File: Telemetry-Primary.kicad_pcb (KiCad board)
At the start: 2 copper layers, 95 x 82 mm, 153 parts, among them J1 CAN_LogicAnalyzer, J10 SMAConn, J11 CAN_In, J12 CAN_Out, J2 IMU_LogicAnalyzer, J3 GPS_LogicAnalyzer, J4 SWD, J5 SDCard_LogicAnalyzer, J6 USB_B_Micro, J7 PowerConn, J8 RJ45_Abracon_ARJP11A-MASA-B-A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, J9 Micro_SD_Card_Det, SW1 Reset, SW2 RTCC_BattCheck, SW3 GPS_BattCheck, U1 STM32F429ZITx, U10 RN4871-I, U11 LAN8742A-CZ-TR, U12 USBLC6-4SC6, U2 RI3-1205S, U3 LD1117-3.3_SOT223, U4 ADM3055E, U5 CDSOT23-T24CAN, U6 BNO055, U7 MTK3339, U8 CP2102N-A02-GQFN24, U9 MCP112, Y1 8M, Y2 25M, Y3 32.768k

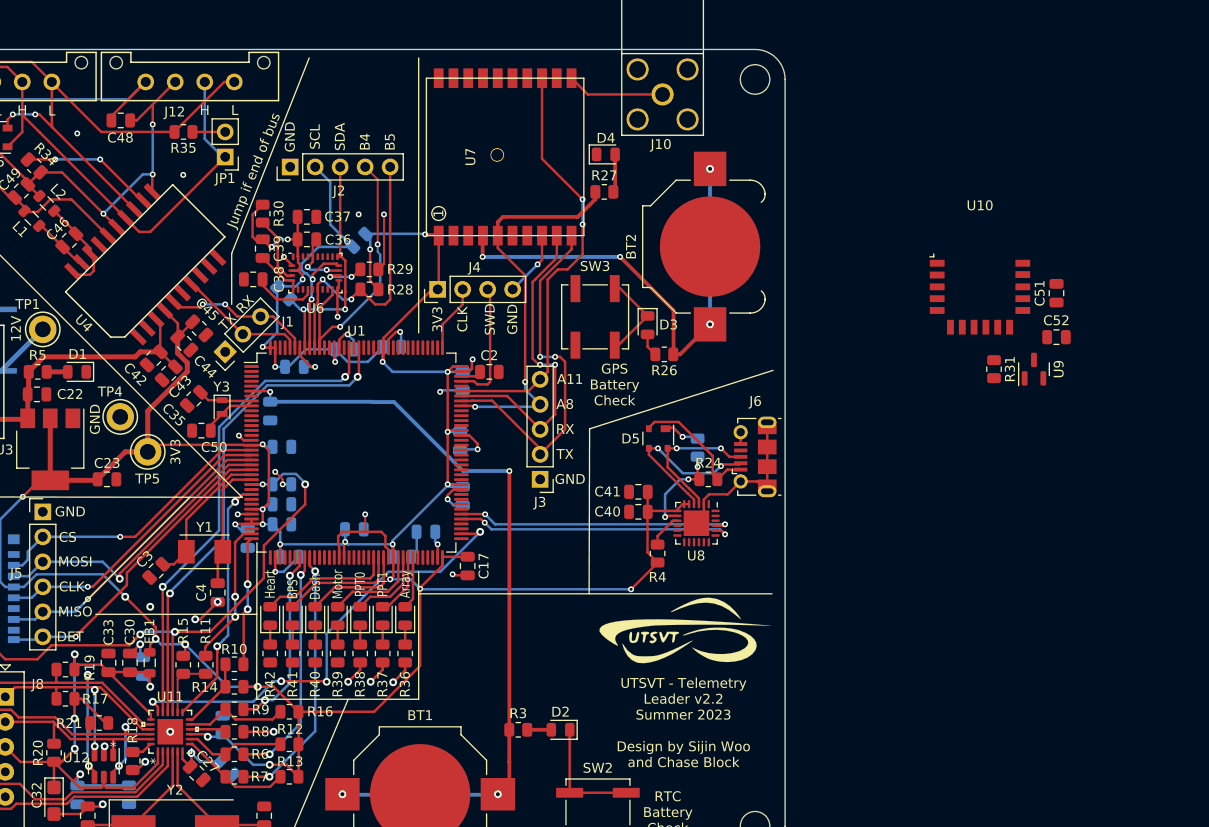
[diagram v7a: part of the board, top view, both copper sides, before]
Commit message: new bt module + preliminary reverse protection
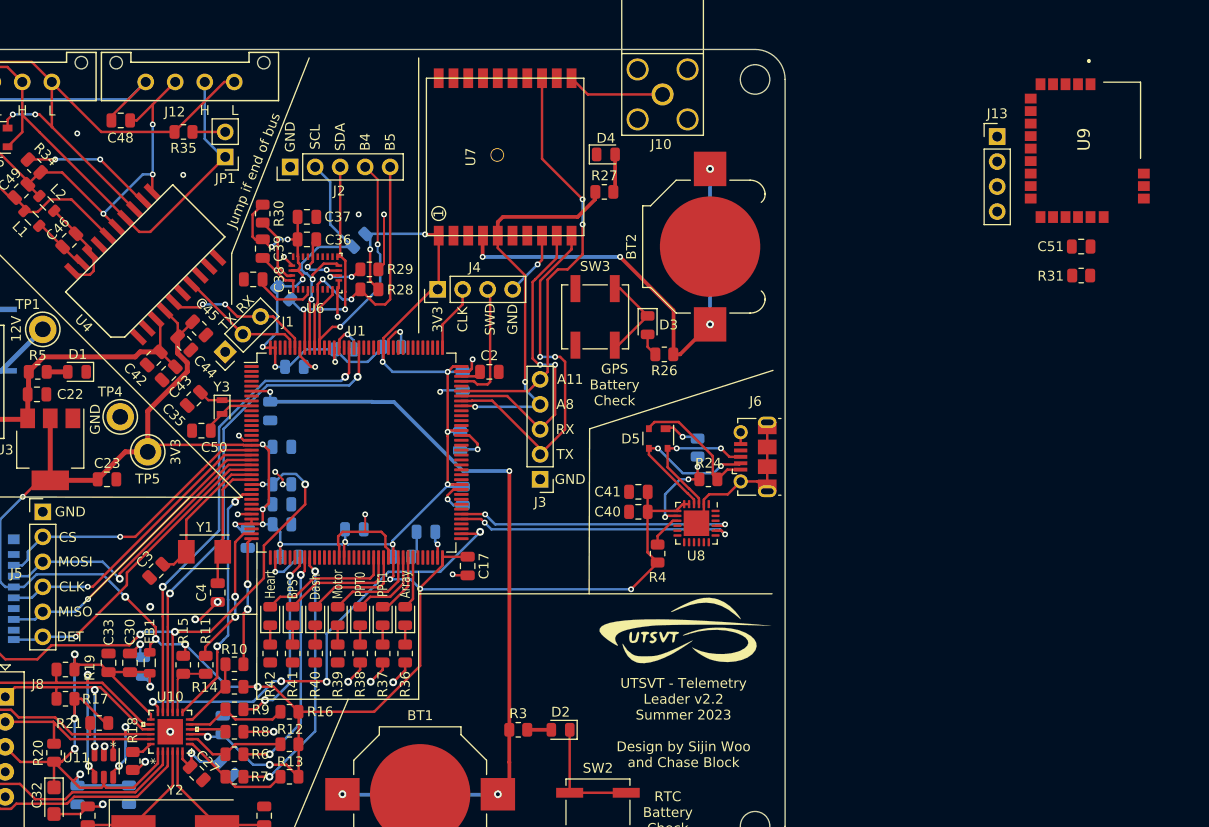
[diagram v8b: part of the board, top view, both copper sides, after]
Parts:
- removed the C51 at (193.7, 69.7)
- removed the U10 at (185.9, 70.1)
- added J13: SWD, Connector_PinHeader_2.54mm:PinHeader_1x04_P2.54mm_Vertical, F.Cu at (187.7, 53.8)
- C51: renamed from C52; value 1u -> 10n
- R31: value 4.7k -> 47k
- U9: value MCP112 -> BLUENRG-M2SA; footprint Package_TO_SOT_SMD:SOT-23 -> UTSVT_ICs:BLUENRGM2SA
- moved U9 23.9 mm to (196.5, 54.1), turned to -90 degrees
- moved R31 13.0 mm to (196.2, 67.9), turned to 0 degrees
- moved C51 9.54 mm to (196.2, 65.0), turned to 180 degrees
- renumbered U11 to U10, U12 to U11
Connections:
- C51 pad 1: Net-(U10-RST) -> Net-(U9-RESETN)
- R31 pad 2: Net-(U10-RST) -> Net-(U9-RESETN)
- U9 pad 1: Net-(U10-RST) -> unconnected-(U9-ADC2-Pad1)
- U9 pad 2: GND -> unconnected-(U9-ADC1-Pad2)
- U9 pad 3: +3.3V -> unconnected-(U9-DIO4-Pad3)
